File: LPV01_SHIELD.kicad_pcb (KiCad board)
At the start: 4 copper layers, 140 x 125 mm, 102 parts, among them J1 Conn_01x02_Pin, J1 Screw_Terminal_01x02, J10 SPI_header, J11 Power_socket, J12 USB1035-GF-P-0-B-B, J13 USB1035-GF-P-0-B-B, J14 USB1035-GF-P-0-B-B, J15 Screw_Terminal_01x03, J16 Screw_Terminal_01x03, J17 Wiegand, J18 A-USBSA, J19 Screw_Terminal_01x02, J2 Conn_01x02_Pin, J2 Screw_Terminal_01x02, J20 Screw_Terminal_01x02, J21 Screw_Terminal_01x02, J22 Screw_Terminal_01x02, J23 GND, J24 Conn_01x02, J3 Conn_01x02_Pin, J3 Screw_Terminal_01x02, J4 Conn_01x02_Pin, J4 Screw_Terminal_01x02, J5 Conn_01x03_Pin, J6 Conn_01x02_Pin, J9 GPIO_header, Q1 BC817, Q2 BC817, Q3 BC817, Q4 BC817, SW1 SW_SPST, SW2 SW_SPST, SW3 SW_SPST, SW4 SW_SPST, U1 MP2491C, U1 TLP175A, U11 AMS1117-3.3, U12 USB2517I-JZX, U13 FT2232HQ, U14 MIC2026-1xM, U15 MIC2026-1xM, U16 M24C02-FMN, U17 MIC2026-1xM, U2 TLP175A, U3 TLP175A, U4 TLP175A, U9 MP2491C

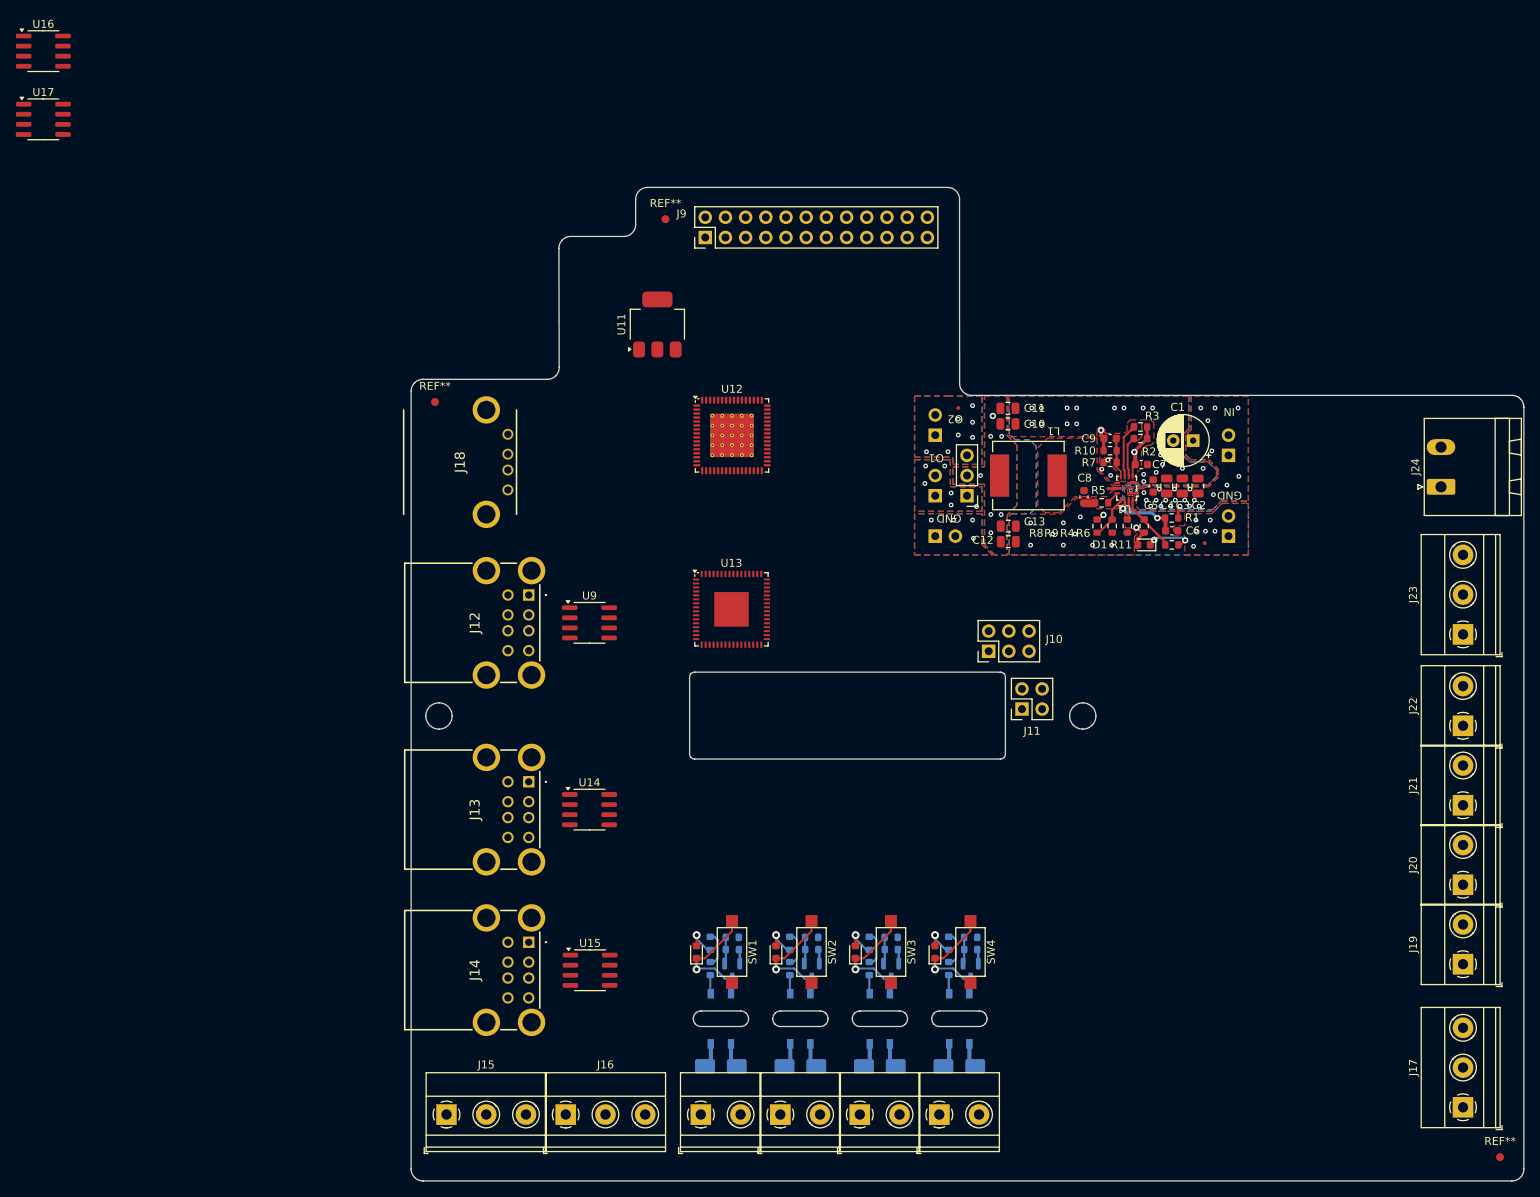
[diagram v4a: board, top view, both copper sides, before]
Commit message: Added 2 schematic sheets
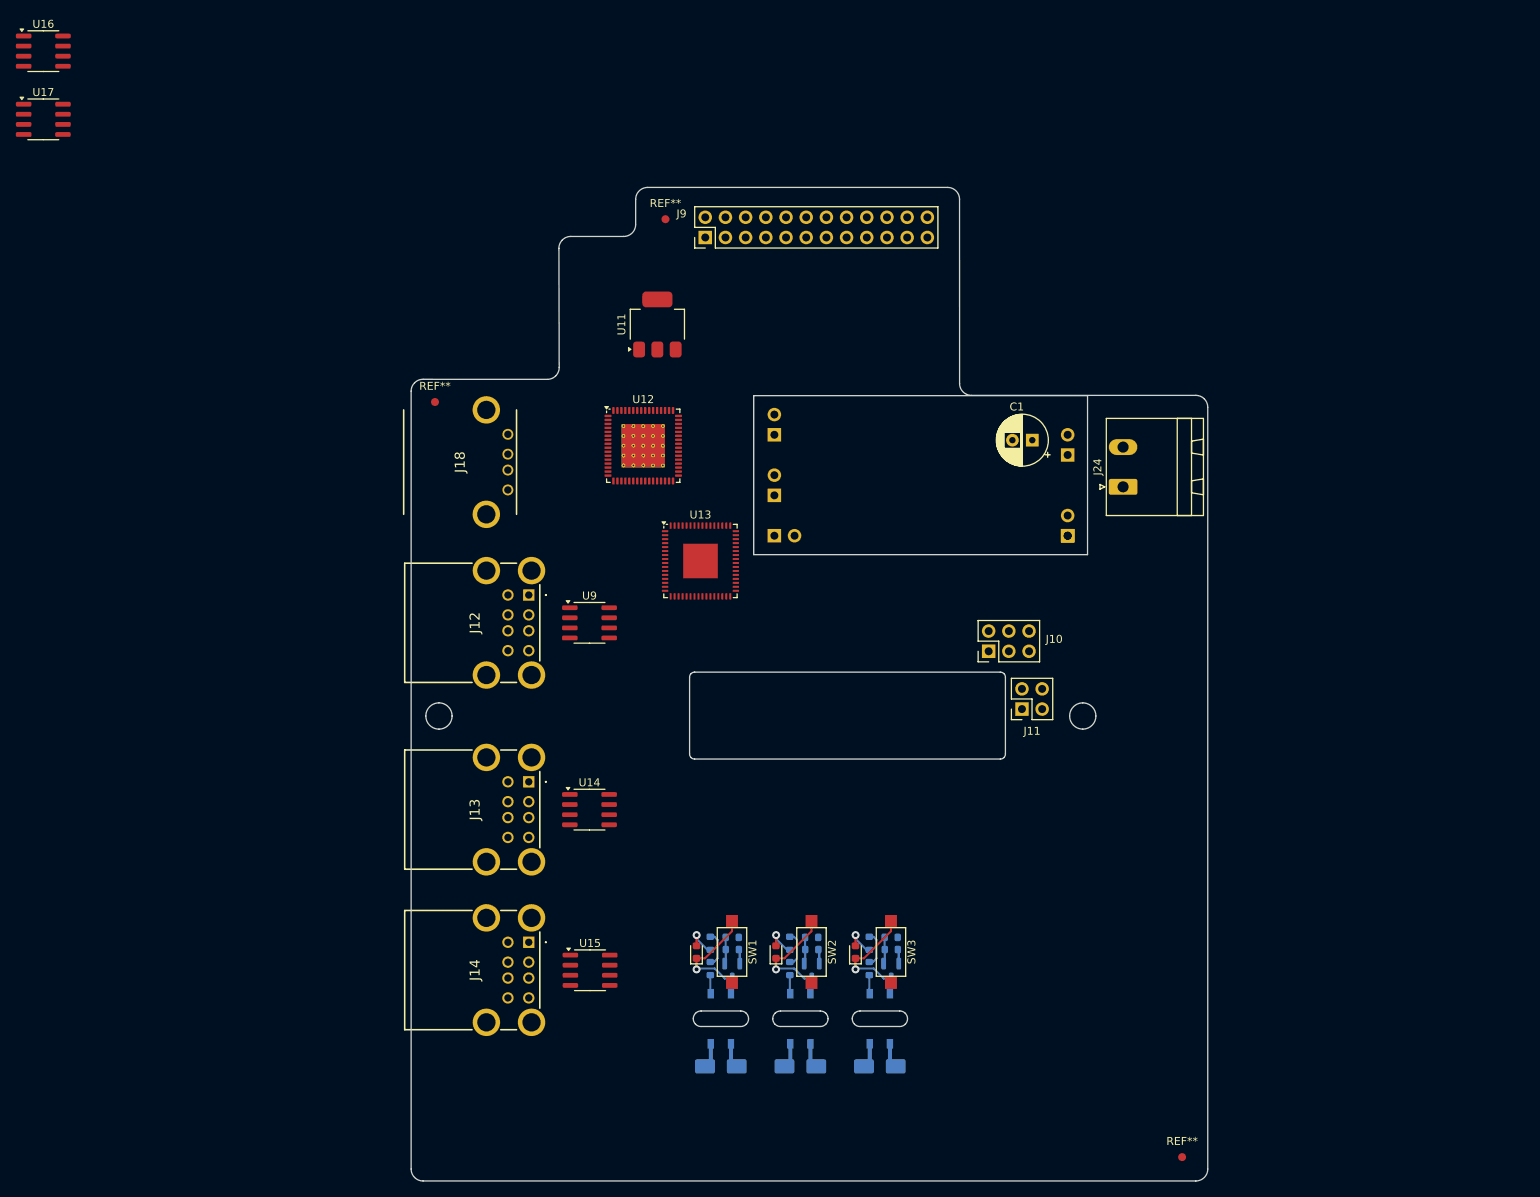
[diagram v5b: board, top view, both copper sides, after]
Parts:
- removed C10, C11, C12, C13: 22u, Capacitor_SMD:C_0805_2012Metric
- removed C2, C3, C4: 10u, Capacitor_SMD:C_0805_2012Metric
- removed C5: 100n, Capacitor_SMD:C_0603_1608Metric
- removed C6: 1n, Capacitor_SMD:C_0603_1608Metric
- removed C7: 2u2, Capacitor_SMD:C_0603_1608Metric
- removed C8: 1u, Capacitor_SMD:C_0603_1608Metric
- removed C9: 22p, Capacitor_SMD:C_0603_1608Metric
- removed the D1 at (142.2, 65.0)
- removed D7: LED, LED_SMD:LED_0603_1608Metric
- removed D8: SMF48CA, Diode_SMD:D_SMA
- removed the J1 at (86.5, 136.6)
- removed the J1 at (152.8, 52.4)
- removed J15, J16: Screw_Terminal_01x03, TerminalBlock_Phoenix:TerminalBlock_Phoenix_MKDS-1,5-3_1x03_P5.00mm_Horizontal
- removed J17: Wiegand, TerminalBlock_Phoenix:TerminalBlock_Phoenix_MKDS-1,5-3_1x03_P5.00mm_Horizontal
- removed J19, J20, J21, J22: Screw_Terminal_01x02, TerminalBlock_Phoenix:TerminalBlock_Phoenix_MKDS-1,5-2_1x02_P5.00mm_Horizontal
- removed the J2 at (96.5, 136.6)
- removed the J2 at (152.8, 62.6)
- removed J23: GND, TerminalBlock_Phoenix:TerminalBlock_Phoenix_MKDS-1,5-3_1x03_P5.00mm_Horizontal
- removed the J3 at (106.5, 136.6)
- removed the J3 at (115.9, 57.5)
- removed the J4 at (116.5, 136.6)
- removed the J4 at (117.2, 63.9)
- removed J5: Conn_01x03_Pin, Connector_PinHeader_2.54mm:PinHeader_1x03_P2.54mm_Vertical
- removed L1: 4u7, HK:Inductor_IHLP3232DZER4R7M11_HK
- removed Q4: BC817, Package_TO_SOT_SMD:SOT-23
- removed the R1 at (145.7, 61.6)
- removed the R10 at (137.9, 53.1)
- removed the R11 at (145.7, 65.0)
- removed R13: 1k, Resistor_SMD:R_0603_1608Metric
- removed R14, R15: 4k7, Resistor_SMD:R_0603_1608Metric
- removed R16: 10k, Resistor_SMD:R_0603_1608Metric
- removed the R2 at (141.8, 51.6)
- removed the R3 at (141.8, 50.1)
- removed the R4 at (140.1, 62.6)
- removed the R5 at (136.9, 59.7)
- removed the R6 at (142.2, 62.6)
- removed the R7 at (137.9, 54.6)
- removed the R8 at (136.3, 62.6)
- removed the R9 at (138.2, 62.6)
- removed the REF** at (118.8, 47.8)
- removed the REF** at (149.8, 64.8)
- removed SW4: SW_SPST, Button_Switch_SMD:SW_SPST_CK_RS282G05A3
- removed the U1 at (140.0, 57.8)
- removed U4: TLP175A, Package_SO:MFSOP6-4_4.4x3.6mm_P1.27mm
- added ?: , , F.Cu at (132.6, 63.8)
- added J1: Conn_01x02_Pin, Connector_PinHeader_2.54mm:PinHeader_1x02_P2.54mm_Vertical, B.Cu at (132.6, 52.4)
- added J2: Conn_01x02_Pin, Connector_PinHeader_2.54mm:PinHeader_1x02_P2.54mm_Vertical, B.Cu at (132.6, 62.5)
- added J3: Conn_01x02_Pin, Connector_PinHeader_2.54mm:PinHeader_1x02_P2.54mm_Vertical, B.Cu at (95.7, 57.5)
- added J4: Conn_01x02_Pin, Connector_PinHeader_2.54mm:PinHeader_1x02_P2.54mm_Vertical, B.Cu at (97.0, 63.8)
- moved J24 40.0 mm to (139.6, 57.7)
- moved REF** 40.0 mm to (147.0, 142.0)
- moved C1 20.2 mm to (126.9, 51.8)
- moved J6 20.2 mm to (95.7, 49.9)
- moved U12 11.2 mm to (79.2, 52.5)
- moved U13 7.22 mm to (86.4, 67.0)
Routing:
- net (no net): track 58.0 -> 0.00 mm, vias 18 -> 0
- net Net-(D7-K): track 15.6 -> 0.00 mm, vias 1 -> 0
- net +5V: track 20.8 -> 13.5 mm, vias 8 -> 0
- net Net-(D1-K): track 21.7 -> 15.6 mm, vias 3 -> 1
- net Net-(D7-A): track 4.12 -> 0.00 mm, vias 1 -> 0
- net Net-(Q4-B): track 3.36 -> 0.00 mm
- net Net-(D8-A1): track 3.33 -> 0.00 mm
- net Net-(D8-A2): track 3.14 -> 0.00 mm
- net Net-(R13-Pad1): track 2.36 -> 0.00 mm
- net GND: track 7.25 -> 5.44 mm, vias 42 -> 0
- net +24V: track 1.30 -> 0.00 mm, vias 26 -> 0
- removed copper zone on B.Cu, net (none)
- removed copper zone on F.Cu, net (none)
- removed copper zone on B.Cu, net +24V
- removed copper zone on F.Cu, net +24V
- removed copper zone on B.Cu, net +5V
- removed copper zone on F.Cu, net +5V
- removed copper zone on B.Cu, net GND
- removed copper zone on F.Cu, net GND
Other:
- board size 140 x 125 mm -> 100.2 x 125 mm
- board text removed: "GND"
- board text removed: "IN"
- board text removed: "O1"
- board text removed: "O2"

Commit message: Added inputs and outputs to the schematic
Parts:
- removed ?: , 
- removed C1: 100u, Capacitor_THT:CP_Radial_D6.3mm_P2.50mm
- removed J1, J2, J3, J4, J6: Conn_01x02_Pin, Connector_PinHeader_2.54mm:PinHeader_1x02_P2.54mm_Vertical
- removed U16: M24C02-FMN, Package_SO:SOIC-8_3.9x4.9mm_P1.27mm
- removed U17: MIC2026-1xM, Package_SO:SOIC-8_3.9x4.9mm_P1.27mm
- added J19: Screw_Terminal_01x02, TerminalBlock_Phoenix:TerminalBlock_Phoenix_MKDS-1,5-2_1x02_P5.00mm_Horizontal, F.Cu at (82.6, 138.9)
- added J20: Screw_Terminal_01x02, TerminalBlock_Phoenix:TerminalBlock_Phoenix_MKDS-1,5-2_1x02_P5.00mm_Horizontal, F.Cu at (94.2, 138.9)
- added J21: Screw_Terminal_01x02, TerminalBlock_Phoenix:TerminalBlock_Phoenix_MKDS-1,5-2_1x02_P5.00mm_Horizontal, F.Cu at (105.8, 138.9)
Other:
- outline, holes or cut-outs redrawn
